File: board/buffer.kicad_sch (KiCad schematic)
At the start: 10 parts, among them J6 Conn_02x03_Odd_Even, J7 Conn_02x03_Odd_Even, SW4 SW_DIP_x04, U5 TXB0104PW (fit with U104)

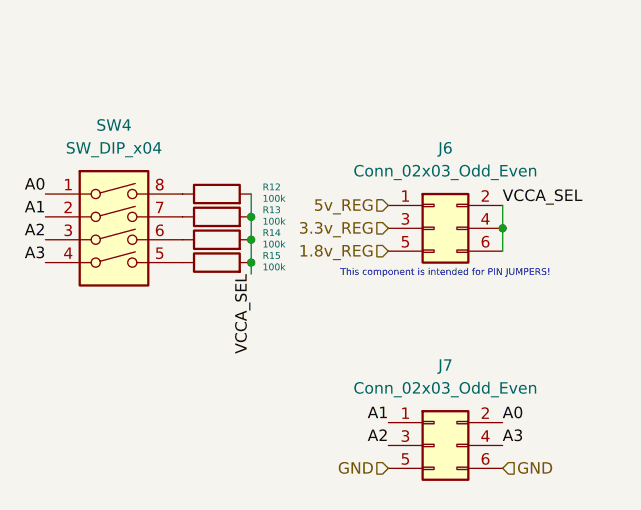
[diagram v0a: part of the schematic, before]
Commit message: 2.0 first commit * started switching caps to standard value of 0603 4.7uF (which is overkill everywhere) * tidied up some silkscreen * replaced 4x100kOhm pullup resistors with 1 array (of the same values) * made some space for the zener clamping circuit (will still be a very tight fit)
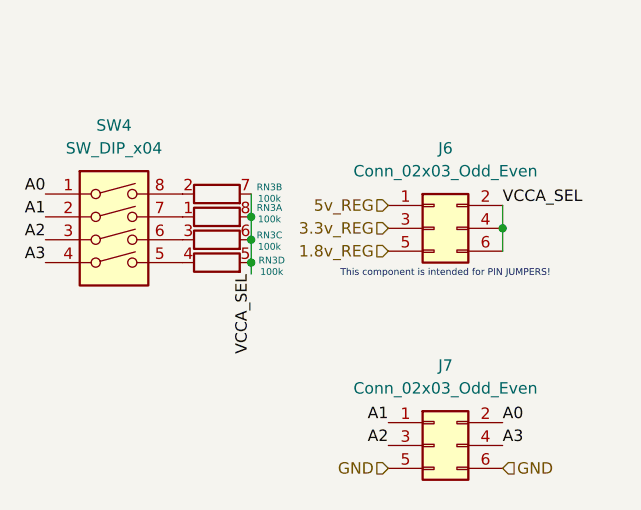
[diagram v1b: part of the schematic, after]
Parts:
- removed R12, R13, R14, R15: 100k, Resistor_SMD:R_0402_1005Metric, symbol Device:R
- added RN3: 100k, Resistor_SMD:R_Array_Convex_4x0402, symbol Device:R_Pack04_SIP_Split
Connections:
- net VCCA_SEL: now also RN3.5 (R4.2), RN3.6 (R3.2), RN3.7 (R2.2), RN3.8 (R1.2)
- net at SW4.5: now also RN3.4 (R4.1)
- net at SW4.7: now also RN3.1 (R1.1)
- net at SW4.6: now also RN3.3 (R3.1)
- net at SW4.8: now also RN3.2 (R2.1)

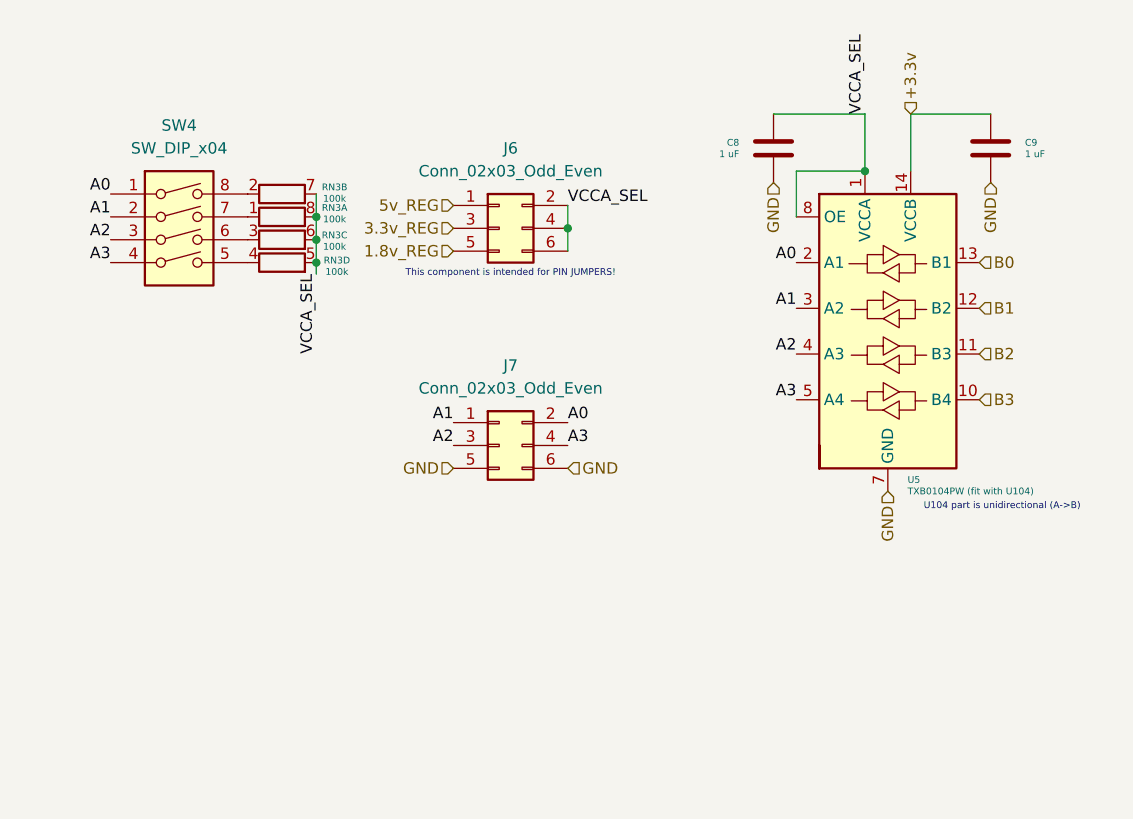
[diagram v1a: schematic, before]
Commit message: add zener diode clamping circuit
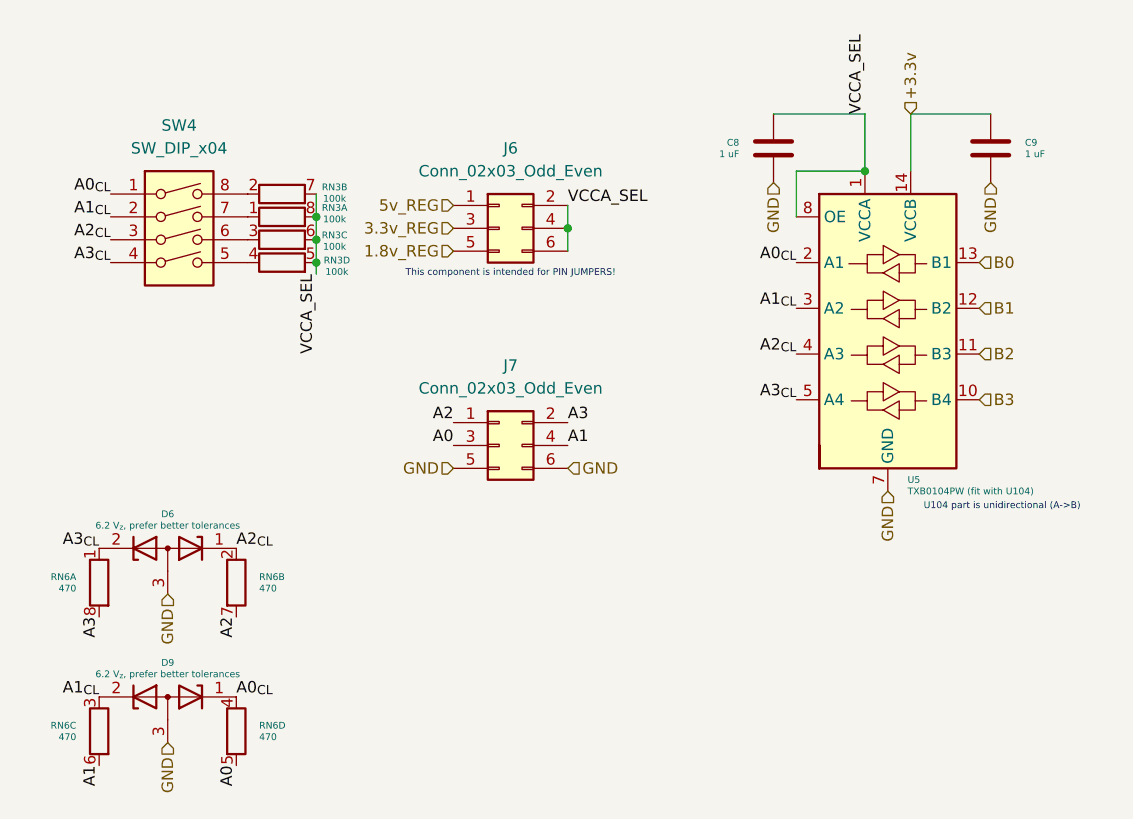
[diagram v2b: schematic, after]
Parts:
- added D6, D9: 6.2 V_{z}, prefer better tolerances, Package_TO_SOT_SMD:SOT-23, symbol Device:D_Zener_Dual_CommonAnode_KKA
- added RN6: 470, Resistor_SMD:R_Array_Convex_4x0402, symbol Device:R_Pack04_SIP_Split
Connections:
- net A0: now also J7.3 (Pin_3), RN6.5 (R4.2); no longer J7.2 (Pin_2), SW4.1, U5.2 (A1)
- net A1: now also J7.4 (Pin_4), RN6.6 (R3.2); no longer J7.1 (Pin_1), SW4.2, U5.3 (A2)
- net A2: now also J7.1 (Pin_1), RN6.7 (rR2.2); no longer J7.3 (Pin_3), SW4.3, U5.4 (A3)
- net A3: now also J7.2 (Pin_2), RN6.8 (R1.2); no longer J7.4 (Pin_4), SW4.4, U5.5 (A4)
- net GND: now also D6.3 (A), D9.3 (A)
- new net A0_{CL}: D9.1 (K), RN6.4 (R4.1), SW4.1, U5.2 (A1)
- new net A1_{CL}: D9.2 (K), RN6.3 (R3.1), SW4.2, U5.3 (A2)
- new net A2_{CL}: D6.1 (K), RN6.2 (R2.1), SW4.3, U5.4 (A3)
- new net A3_{CL}: D6.2 (K), RN6.1 (R1.1), SW4.4, U5.5 (A4)

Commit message: layout overhaul backside pico now, which significantly reduces the size of the board and lets me do less suspect routing need to finish power delivery network for 3.3v, 5v reference, and 1.8v reference rails
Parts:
- removed C9: 1 uF, Capacitor_SMD:C_0402_1005Metric, symbol Device:C
- added C5: 4.7 uF, Capacitor_SMD:C_0603_1608Metric, symbol Device:C
- C8: value 1 uF -> 4.7 uF; footprint Capacitor_SMD:C_0402_1005Metric -> Capacitor_SMD:C_0603_1608Metric
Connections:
- net +3.3v: now also U5.8 (OE), C5.2
- net 1.8v_REG: now also J6.3 (Pin_3); no longer J6.5 (Pin_5)
- net 3.3v_REG: now also J6.1 (Pin_1); no longer J6.3 (Pin_3)
- net 5v_REG: now also J6.5 (Pin_5); no longer J6.1 (Pin_1)
- net A0: now also J7.1 (Pin_1); no longer J7.3 (Pin_3)
- net A1: now also J7.2 (Pin_2); no longer J7.4 (Pin_4)
- net A2: now also J7.3 (Pin_3); no longer J7.1 (Pin_1)
- net A3: now also J7.4 (Pin_4); no longer J7.2 (Pin_2)
- net GND: now also C5.1
- net VCCA_SEL: no longer U5.8 (OE)
- net at RN3.3 (R3.1): now also SW4.7; no longer SW4.6
- net at RN3.2 (R2.1): now also SW4.6; no longer SW4.8
- net at RN3.1 (R1.1): now also SW4.5; no longer SW4.7
- net at RN3.4 (R4.1): now also SW4.8; no longer SW4.5
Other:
- moved on the sheet: RN3A, RN3B, RN3C, RN3D

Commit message: finish power routing also 9.0 import! jobsets coming soon
export is very broken at this point, do not trust the artifacts
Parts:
- renumbered C8 to C4, D6 to D4, D9 to D7, J6 to J2, J7 to J3, RN3 to RN1, RN6 to RN4, SW4 to SW2, U5 to U3
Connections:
- net 1.8v_REG: now also J2.1 (Pin_1); no longer J2.3 (Pin_3)
- net 3.3v_REG: now also J2.5 (Pin_5); no longer J2.1 (Pin_1)
- net 5v_REG: now also J2.3 (Pin_3); no longer J2.5 (Pin_5)
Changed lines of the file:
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@@
 (kicad_sch
-	(version 20231120)
+	(version 20250114)
 	(generator "eeschema")
-	(generator_version "8.0")
+	(generator_version "9.0")
 	(paper "A4")
+	(text "This component is intended for PIN JUMPERS!"
+		(exclude_from_sim no)
+		(at 89.408 89.662 0)
+		(effects
+			(font
+				(size 0.75 0.75)
+			)
+		)
+	)
+	(text "U104 part is unidirectional (A->B)"
+		(exclude_from_sim no)
+		(at 143.51 113.538 0)
+		(effects
+			(font
+				(size 0.75 0.75)
+			)
+		)
+	)
 	(junction
 		(at 95.25 85.09)
@@
 		)
 	)
-	(text "This component is intended for PIN JUMPERS!"
-		(exclude_from_sim no)
-		(at 89.408 89.662 0)
-		(effects
-			(font
-				(size 0.75 0.75)
-			)
-		)
-	)
-	(text "U104 part is unidirectional (A->B)"
-		(exclude_from_sim no)
-		(at 143.51 113.538 0)
-		(effects
-			(font
-				(size 0.75 0.75)
-			)
-		)
-	)
 	(label "VCCA_SEL"
 		(at 95.25 80.01 0)
@@
 		)
 	)
+	(hierarchical_label "5v_REG"
+		(shape input)
+		(at 82.55 82.55 180)
+		(effects
+			(font
+				(size 1.27 1.27)
+			)
+			(justify right)
+		)
+	)
 	(hierarchical_label "B2"
 		(shape input)
@@
 		)
 	)
+	(hierarchical_label "3.3v_REG"
+		(shape input)
+		(at 82.55 85.09 180)
+		(effects
+			(font
+				(size 1.27 1.27)
+			)
+			(justify right)
+		)
+	)
 	(hierarchical_label "GND"
 		(shape input)
@@
 		)
 	)
-	(hierarchical_label "3.3v_REG"
-		(shape input)
-		(at 82.55 80.01 180)
-		(effects
-			(font
-				(size 1.27 1.27)
-			)
-			(justify right)
-		)
-	)
 	(hierarchical_label "GND"
 		(shape input)
@@
 		)
 	)
-	(hierarchical_label "5v_REG"
-		(shape input)
-		(at 82.55 85.09 180)
-		(effects
-			(font
-				(size 1.27 1.27)
-			)
-			(justify right)
-		)
-	)
 	(hierarchical_label "GND"
 		(shape input)
@@
 		)
 	)
-	(hierarchical_label "1.8v_REG"
-		(shape input)
-		(at 82.55 82.55 180)
-		(effects
-			(font
-				(size 1.27 1.27)
-			)
-			(justify right)
-		)
-	)
 	(hierarchical_label "+3.3v"
 		(shape input)
@@
 			)
 			(justify left)
+		)
+	)
+	(hierarchical_label "1.8v_REG"
+		(shape input)
+		(at 82.55 80.01 180)
+		(effects
+			(font
+				(size 1.27 1.27)
+			)
+			(justify right)
 		)
 	)
@@
 		(on_board yes)
 		(dnp no)
-		(property "Reference" "RN3"
+		(property "Reference" "RN1"
 			(at 69.342 80.772 90)
 			(effects
@@
 		(dnp no)
 		(fields_autoplaced yes)
-		(property "Reference" "J7"
+		(property "Reference" "J3"
 			(at 88.9 97.79 0)
 			(effects
@@
 		(on_board yes)
 		(dnp no)
-		(property "Reference" "RN3"
+		(property "Reference" "RN1"
 			(at 69.342 83.058 90)
 			(effects
@@
 		(on_board yes)
 		(dnp no)
-		(property "Reference" "C8"
+		(property "Reference" "C4"
 			(at 114.3 73.0249 0)
 			(effects
@@
 		(on_board yes)
 		(dnp no)
-		(property "Reference" "RN3"
+		(property "Reference" "RN1"
 			(at 69.342 85.344 90)
 			(effects
@@
 		(on_board yes)
 		(dnp no)
-		(property "Reference" "RN6"
+		(property "Reference" "RN4"
 			(at 40.64 121.2849 0)
 			(effects
@@
 		(dnp no)
 		(fields_autoplaced yes)
-		(property "Reference" "U5"
+		(property "Reference" "U3"
 			(at 133.0041 110.49 0)
 			(effects
@@
 		(on_board yes)
 		(dnp no)
-		(property "Reference" "RN6"
+		(property "Reference" "RN4"
 			(at 60.96 121.2849 0)
 			(effects
@@
 		(on_board yes)
 		(dnp no)
-		(property "Reference" "RN6"
+		(property "Reference" "RN4"
 			(at 60.96 137.7949 0)
 			(effects
@@
 		(on_board yes)
 		(dnp no)
-		(property "Reference" "RN3"
+		(property "Reference" "RN1"
 			(at 69.342 78.486 90)
 			(effects
@@
 		(on_board yes)
 		(dnp no)
-		(property "Reference" "D6"
+		(property "Reference" "D4"
 			(at 50.8 114.3 0)
 			(effects
@@
 		(dnp no)
 		(fields_autoplaced yes)
-		(property "Reference" "J6"
+		(property "Reference" "J2"
 			(at 88.9 73.66 0)
 			(effects
@@
 		(dnp no)
 		(fields_autoplaced yes)
-		(property "Reference" "SW4"
+		(property "Reference" "SW2"
 			(at 52.07 71.12 0)
 			(effects
@@
 		(on_board yes)
 		(dnp no)
-		(property "Reference" "RN6"
+		(property "Reference" "RN4"
 			(at 40.64 137.7949 0)
 			(effects
@@
 		(on_board yes)
 		(dnp no)
-		(property "Reference" "D9"
+		(property "Reference" "D7"
 			(at 50.8 130.81 0)
 			(effects

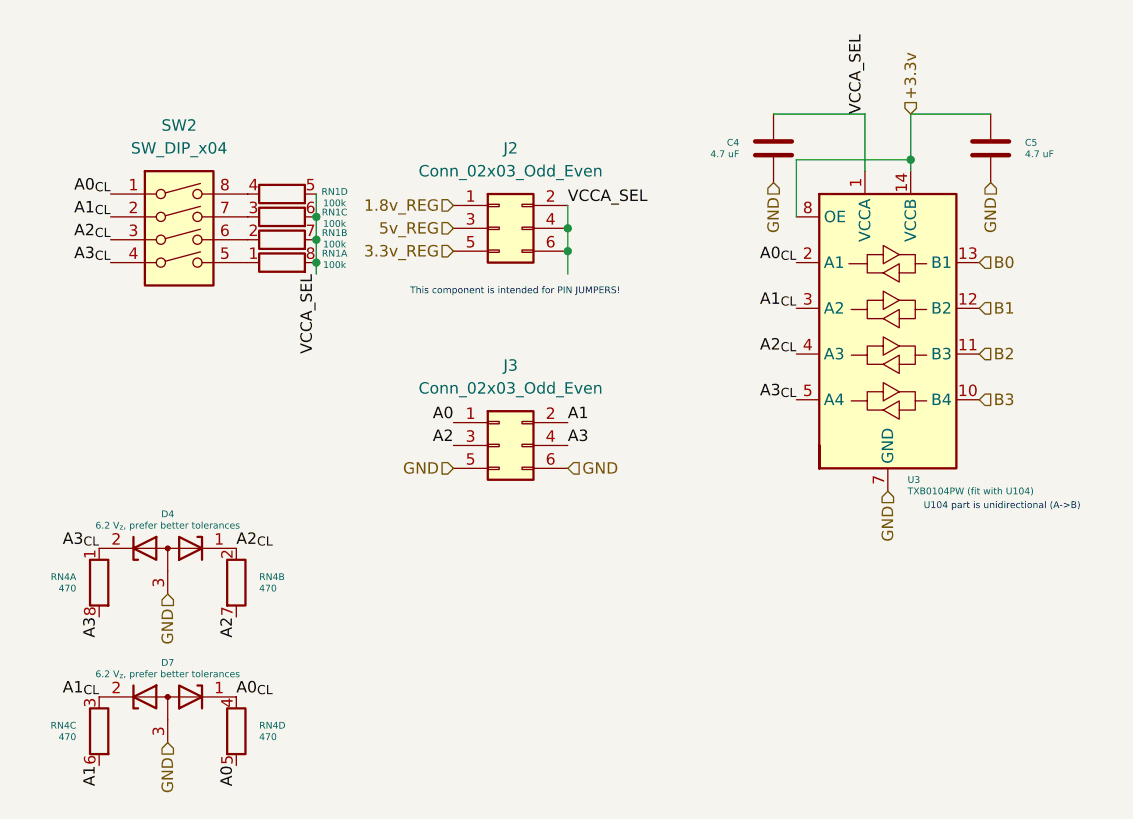
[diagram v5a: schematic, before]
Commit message: backup commit before project structure overhaul
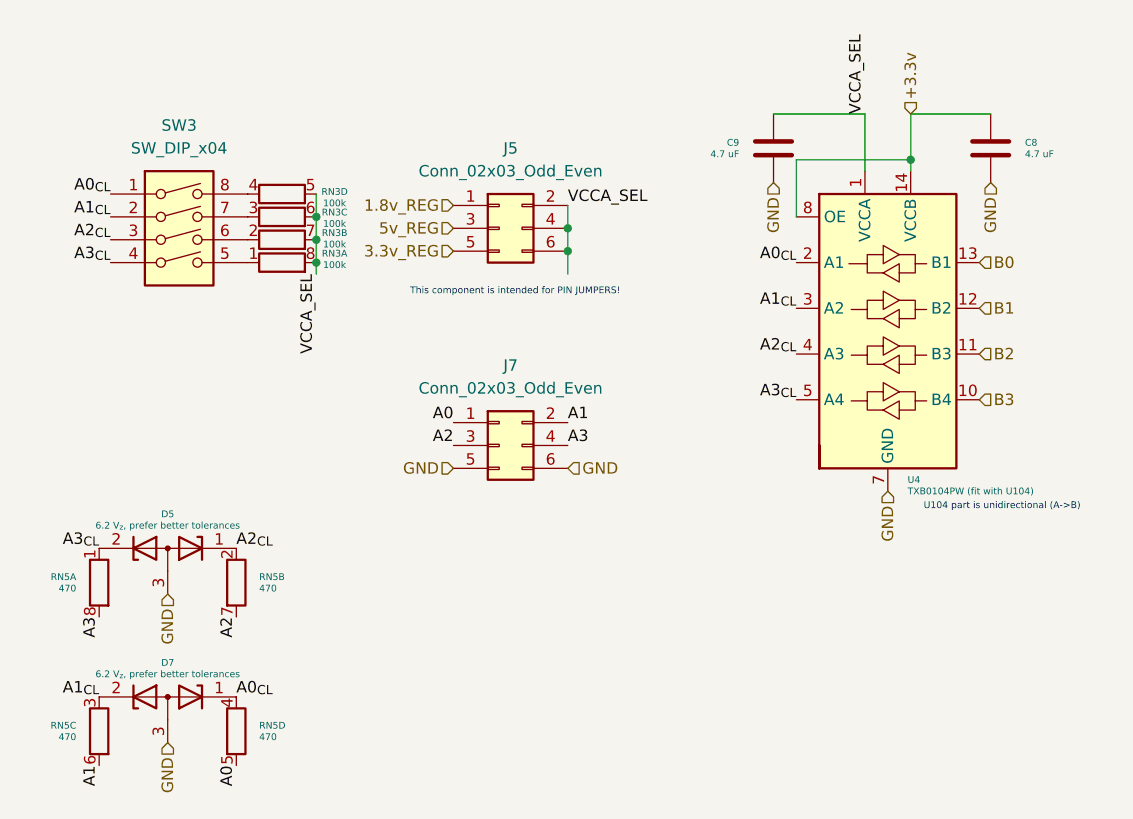
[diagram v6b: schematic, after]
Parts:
- renumbered C5 to C8, C4 to C9, D4 to D5, J2 to J5, J3 to J7, RN1 to RN3, RN4 to RN5, SW2 to SW3, U3 to U4
